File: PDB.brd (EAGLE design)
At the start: 130.3 x 166.9 mm, 55 parts, among them J1 B06B-HCMKK, J2 B06B-HCMKK, J3 SS-6488-NF-A431, J4 SS-6488-NF-A431, J5 B06B-HCMKK, J6 B03B-HCMKS, J7 B03B-HCMKS, J8 SS-6488-NF-A431

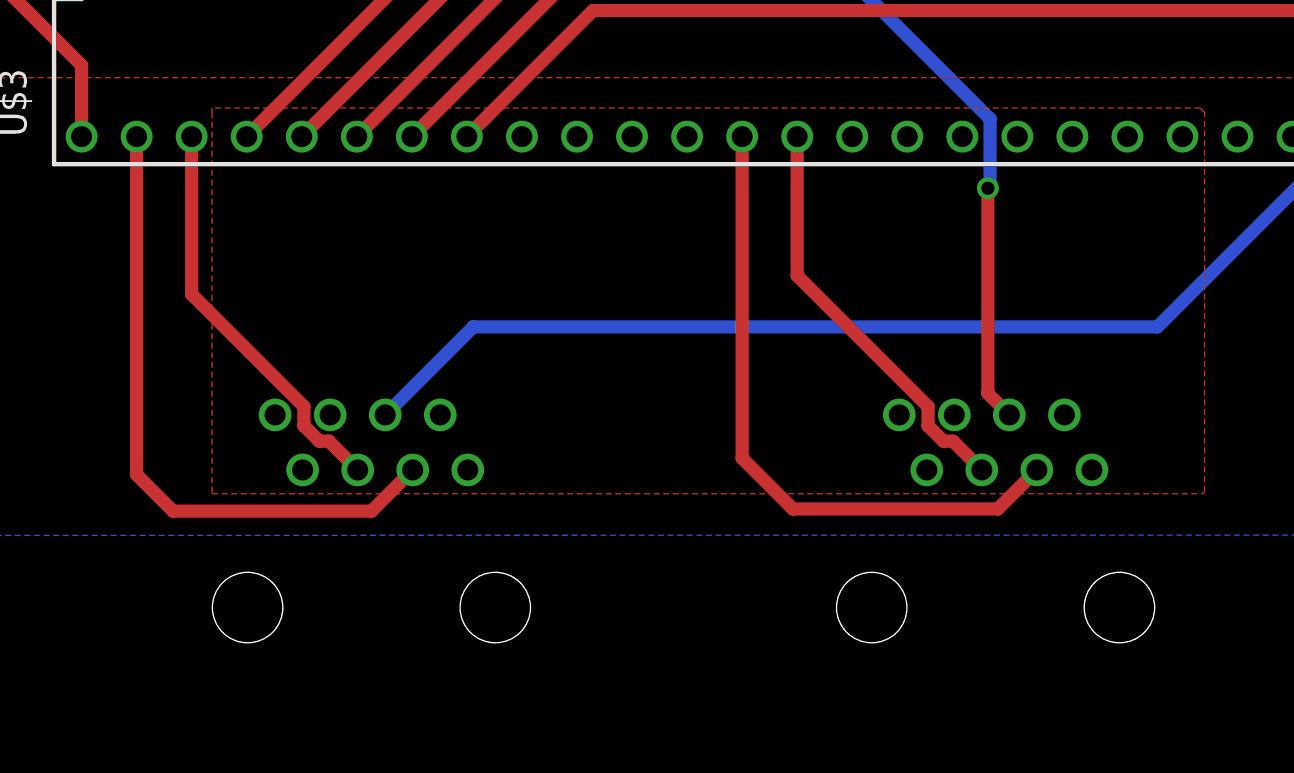
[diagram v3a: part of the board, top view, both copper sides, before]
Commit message: Adjusted schematic and routing to pass twisted pairs to each signal
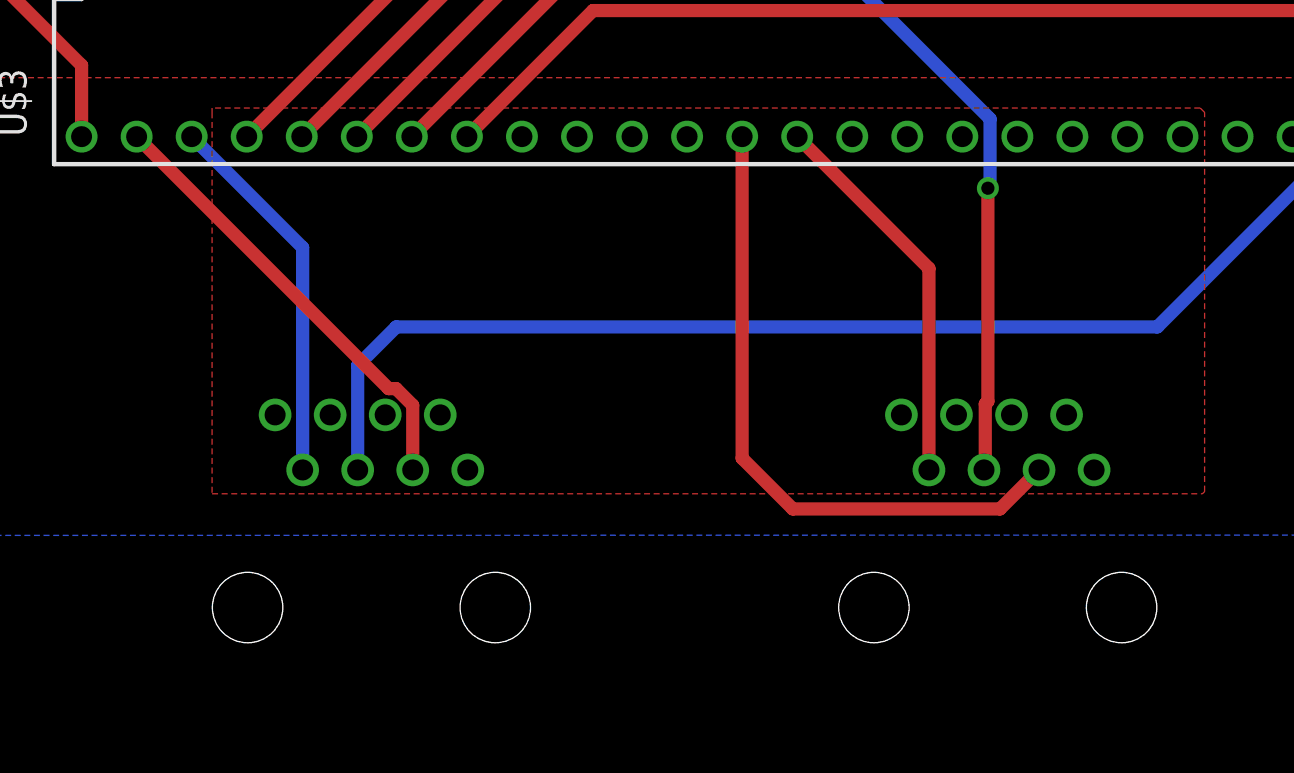
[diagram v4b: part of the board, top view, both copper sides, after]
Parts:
- moved J4 0.10 mm to (86.2, 6.70)
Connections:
- net CLK_A: now also J3.5; no longer J3.4
- net CLK_B: now also J4.5; no longer J4.4
- net GND: now also J3.4, J3.6, J3.8, J4.4, J4.6, J4.8
- net MISO_A: now also J3.7; no longer J3.5
- net MISO_B: now also J4.7; no longer J4.5
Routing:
- net MOSI_A: track 29.8 -> 20.9 mm
- net CLK_A: track 49.7 -> 54.9 mm
- net CLK_B: track 32.2 -> 34.4 mm
- net MISO_A: track 18.8 -> 17.5 mm
- net MISO_B: track 19.2 -> 17.9 mm
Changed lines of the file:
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@@
 <drawing>
 <settings>
-<setting alwaysvectorfont="no"/>
+<setting alwaysvectorfont="yes"/>
 <setting verticaltext="up"/>
 </settings>
@@
 <attribute name="VALUE" x="53.165" y="0.16" size="1.27" layer="28" rot="MR0" align="center"/>
 </element>
-<element name="J4" library="AUX Lib" package="SS6488NFA431" value="SS-6488-NF-A431" x="86.1" y="6.7" smashed="yes" rot="MR0">
-<attribute name="DESCRIPTION" value="Modular Connectors / Ethernet Connectors RJ45 Connector" x="86.1" y="6.7" size="1.778" layer="28" rot="MR0" display="off"/>
-<attribute name="HEIGHT" value="12.82mm" x="86.1" y="6.7" size="1.778" layer="28" rot="MR0" display="off"/>
-<attribute name="MANUFACTURER_NAME" value="Bel" x="86.1" y="6.7" size="1.778" layer="28" rot="MR0" display="off"/>
-<attribute name="MANUFACTURER_PART_NUMBER" value="SS-6488-NF-A431" x="86.1" y="6.7" size="1.778" layer="28" rot="MR0" display="off"/>
-<attribute name="MOUSER_PART_NUMBER" value="530-SS-6488-NF-A431" x="86.1" y="6.7" size="1.778" layer="28" rot="MR0" display="off"/>
-<attribute name="MOUSER_PRICE-STOCK" value="" x="86.1" y="6.7" size="1.778" layer="28" rot="MR0" display="off"/>
-<attribute name="NAME" x="81.965" y="0.16" size="1.27" layer="26" rot="MR0" align="center"/>
-<attribute name="VALUE" x="81.965" y="0.16" size="1.27" layer="28" rot="MR0" align="center"/>
+<element name="J4" library="AUX Lib" package="SS6488NFA431" value="SS-6488-NF-A431" x="86.2" y="6.7" smashed="yes" rot="MR0">
+<attribute name="DESCRIPTION" value="Modular Connectors / Ethernet Connectors RJ45 Connector" x="86.2" y="6.7" size="1.778" layer="28" rot="MR0" display="off"/>
+<attribute name="HEIGHT" value="12.82mm" x="86.2" y="6.7" size="1.778" layer="28" rot="MR0" display="off"/>
+<attribute name="MANUFACTURER_NAME" value="Bel" x="86.2" y="6.7" size="1.778" layer="28" rot="MR0" display="off"/>
+<attribute name="MANUFACTURER_PART_NUMBER" value="SS-6488-NF-A431" x="86.2" y="6.7" size="1.778" layer="28" rot="MR0" display="off"/>
+<attribute name="MOUSER_PART_NUMBER" value="530-SS-6488-NF-A431" x="86.2" y="6.7" size="1.778" layer="28" rot="MR0" display="off"/>
+<attribute name="MOUSER_PRICE-STOCK" value="" x="86.2" y="6.7" size="1.778" layer="28" rot="MR0" display="off"/>
+<attribute name="NAME" x="82.065" y="0.16" size="1.27" layer="26" rot="MR0" align="center"/>
+<attribute name="VALUE" x="82.065" y="0.16" size="1.27" layer="28" rot="MR0" align="center"/>
 </element>
 <element name="J5" library="AUX Lib" package="B06BHCMKK" value="B06B-HCMKK" x="92.1" y="54.4" smashed="yes" rot="MR0">
@@
 <wire x1="59.9" y1="142.3" x2="59.9" y2="143.34635" width="1.27" layer="16"/>
 <wire x1="59.9" y1="143.34635" x2="56.19535" y2="147.051" width="1.27" layer="16"/>
-<wire x1="27.4532" y1="115.1" x2="29.55" y2="117.8" width="0" layer="19" extent="1-1"/>
-<wire x1="12.14" y1="89.33" x2="27.4532" y2="115.1" width="0" layer="19" extent="1-1"/>
-<wire x1="12.3" y1="81.512" x2="12.14" y2="89.33" width="0" layer="19" extent="1-1"/>
-<wire x1="12.3" y1="76.432" x2="12.3" y2="81.512" width="0" layer="19" extent="1-1"/>
 </signal>
 <signal name="HAZ_L_SIG">
@@
 <wire x1="112.8" y1="48.05" x2="109.967" y2="48.05" width="1.27" layer="1"/>
 <wire x1="109.967" y1="48.05" x2="109.914" y2="48.103" width="1.27" layer="1"/>
+<contactref element="J3" pad="4"/>
+<contactref element="J3" pad="6"/>
+<contactref element="J3" pad="8"/>
+<contactref element="J4" pad="4"/>
+<contactref element="J4" pad="6"/>
+<contactref element="J4" pad="8"/>
 </signal>
 <signal name="AGND">
@@
 <wire x1="45.61" y1="107.72218125" x2="67.68781875" y2="129.8" width="1.5" layer="16"/>
 <wire x1="67.68781875" y1="129.8" x2="84.40898125" y2="129.8" width="1.5" layer="16"/>
-<wire x1="33.588" y1="49.7" x2="38.668" y2="49.7" width="0" layer="19" extent="1-1"/>
-<wire x1="33.6" y1="52.65" x2="33.588" y2="49.7" width="0" layer="19" extent="1-1"/>
-<wire x1="31.2" y1="51.8" x2="33.6" y2="52.65" width="0" layer="19" extent="1-1"/>
 </signal>
 <signal name="N$10">
@@
 <contactref element="J3" pad="3"/>
 <contactref element="U$3" pad="0"/>
-<wire x1="42.02" y1="22.08" x2="42.02" y2="6.48" width="0.6096" layer="1"/>
-<wire x1="42.02" y1="6.48" x2="43.7" y2="4.8" width="0.6096" layer="1"/>
-<wire x1="43.7" y1="4.8" x2="52.86" y2="4.8" width="0.6096" layer="1"/>
-<wire x1="52.86" y1="4.8" x2="54.76" y2="6.7" width="0.6096" layer="1"/>
+<wire x1="42.02" y1="22.08" x2="53.6483" y2="10.4517" width="0.6096" layer="1"/>
+<wire x1="53.6483" y1="10.4517" x2="53.99190625" y2="10.4517" width="0.6096" layer="1"/>
+<wire x1="53.99190625" y1="10.4517" x2="54.76" y2="9.68360625" width="0.6096" layer="1"/>
+<wire x1="54.76" y1="9.68360625" x2="54.76" y2="6.7" width="0.6096" layer="1"/>
 </signal>
 <signal name="CLK_A">
-<contactref element="J3" pad="4"/>
 <contactref element="U$3" pad="32"/>
 <wire x1="97.9" y1="22.08" x2="89.12" y2="13.3" width="0.6096" layer="16"/>
-<wire x1="57.55" y1="13.3" x2="53.49" y2="9.24" width="0.6096" layer="16"/>
-<wire x1="89.12" y1="13.3" x2="57.55" y2="13.3" width="0.6096" layer="16"/>
+<contactref element="J3" pad="5"/>
+<wire x1="52.22" y1="11.52" x2="52.22" y2="6.7" width="0.6096" layer="16"/>
+<wire x1="89.12" y1="13.3" x2="54" y2="13.3" width="0.6096" layer="16"/>
+<wire x1="54" y1="13.3" x2="52.22" y2="11.52" width="0.6096" layer="16"/>
 </signal>
 <signal name="MISO_A">
-<contactref element="J3" pad="5"/>
 <contactref element="U$3" pad="1"/>
-<wire x1="49.7383" y1="8.73809375" x2="50.44809375" y2="8.0283" width="0.6096" layer="1"/>
-<wire x1="50.44809375" y1="8.0283" x2="50.8917" y2="8.0283" width="0.6096" layer="1"/>
-<wire x1="50.8917" y1="8.0283" x2="52.22" y2="6.7" width="0.6096" layer="1"/>
-<wire x1="44.56" y1="22.08" x2="44.56" y2="14.80360625" width="0.6096" layer="1"/>
-<wire x1="44.56" y1="14.80360625" x2="49.7383" y2="9.62530625" width="0.6096" layer="1"/>
-<wire x1="49.7383" y1="9.62530625" x2="49.7383" y2="8.73809375" width="0.6096" layer="1"/>
+<contactref element="J3" pad="7"/>
+<wire x1="44.56" y1="22.08" x2="49.68" y2="16.96" width="0.6096" layer="16"/>
+<wire x1="49.68" y1="16.96" x2="49.68" y2="6.7" width="0.6096" layer="16"/>
 </signal>
 <signal name="MOSI_B">
@@
 <wire x1="69.96" y1="22.08" x2="69.96" y2="7.24" width="0.6096" layer="1"/>
 <wire x1="69.96" y1="7.24" x2="72.3" y2="4.9" width="0.6096" layer="1"/>
-<wire x1="72.3" y1="4.9" x2="81.76" y2="4.9" width="0.6096" layer="1"/>
-<wire x1="81.76" y1="4.9" x2="83.56" y2="6.7" width="0.6096" layer="1"/>
+<wire x1="72.3" y1="4.9" x2="81.86" y2="4.9" width="0.6096" layer="1"/>
+<wire x1="81.86" y1="4.9" x2="83.66" y2="6.7" width="0.6096" layer="1"/>
 </signal>
 <signal name="MISO_B">
-<contactref element="J4" pad="5"/>
 <contactref element="U$3" pad="12"/>
-<wire x1="78.5383" y1="8.73809375" x2="79.24809375" y2="8.0283" width="0.6096" layer="1"/>
-<wire x1="79.24809375" y1="8.0283" x2="79.6917" y2="8.0283" width="0.6096" layer="1"/>
-<wire x1="79.6917" y1="8.0283" x2="81.02" y2="6.7" width="0.6096" layer="1"/>
-<wire x1="72.5" y1="22.08" x2="72.5" y2="15.66360625" width="0.6096" layer="1"/>
-<wire x1="72.5" y1="15.66360625" x2="78.5383" y2="9.62530625" width="0.6096" layer="1"/>
-<wire x1="78.5383" y1="9.62530625" x2="78.5383" y2="8.73809375" width="0.6096" layer="1"/>
+<contactref element="J4" pad="7"/>
+<wire x1="72.5" y1="22.08" x2="78.58" y2="16" width="0.6096" layer="1"/>
+<wire x1="78.58" y1="16" x2="78.58" y2="6.7" width="0.6096" layer="1"/>
 </signal>
 <signal name="CLK_B">
-<contactref element="J4" pad="4"/>
 <contactref element="U$3" pad="13"/>
 <wire x1="72.5" y1="37.32" x2="72.5" y2="31.8" width="0.6096" layer="16"/>
@@
 <wire x1="81.4" y1="19.8" x2="81.3" y2="19.7" width="0.6096" layer="16"/>
 <via x="81.3" y="19.7" extent="1-16" drill="0.6096"/>
-<wire x1="81.3" y1="19.7" x2="81.3" y2="10.23" width="0.6096" layer="1"/>
-<wire x1="81.3" y1="10.23" x2="82.29" y2="9.24" width="0.6096" layer="1"/>
+<contactref element="J4" pad="5"/>
+<wire x1="81.3" y1="19.7" x2="81.3" y2="9.86360625" width="0.6096" layer="1"/>
+<wire x1="81.3" y1="9.86360625" x2="81.1783" y2="9.74190625" width="0.6096" layer="1"/>
+<wire x1="81.1783" y1="6.7583" x2="81.12" y2="6.7" width="0.6096" layer="1"/>
+<wire x1="81.1783" y1="9.74190625" x2="81.1783" y2="6.7583" width="0.6096" layer="1"/>
 </signal>
 <signal name="H9">

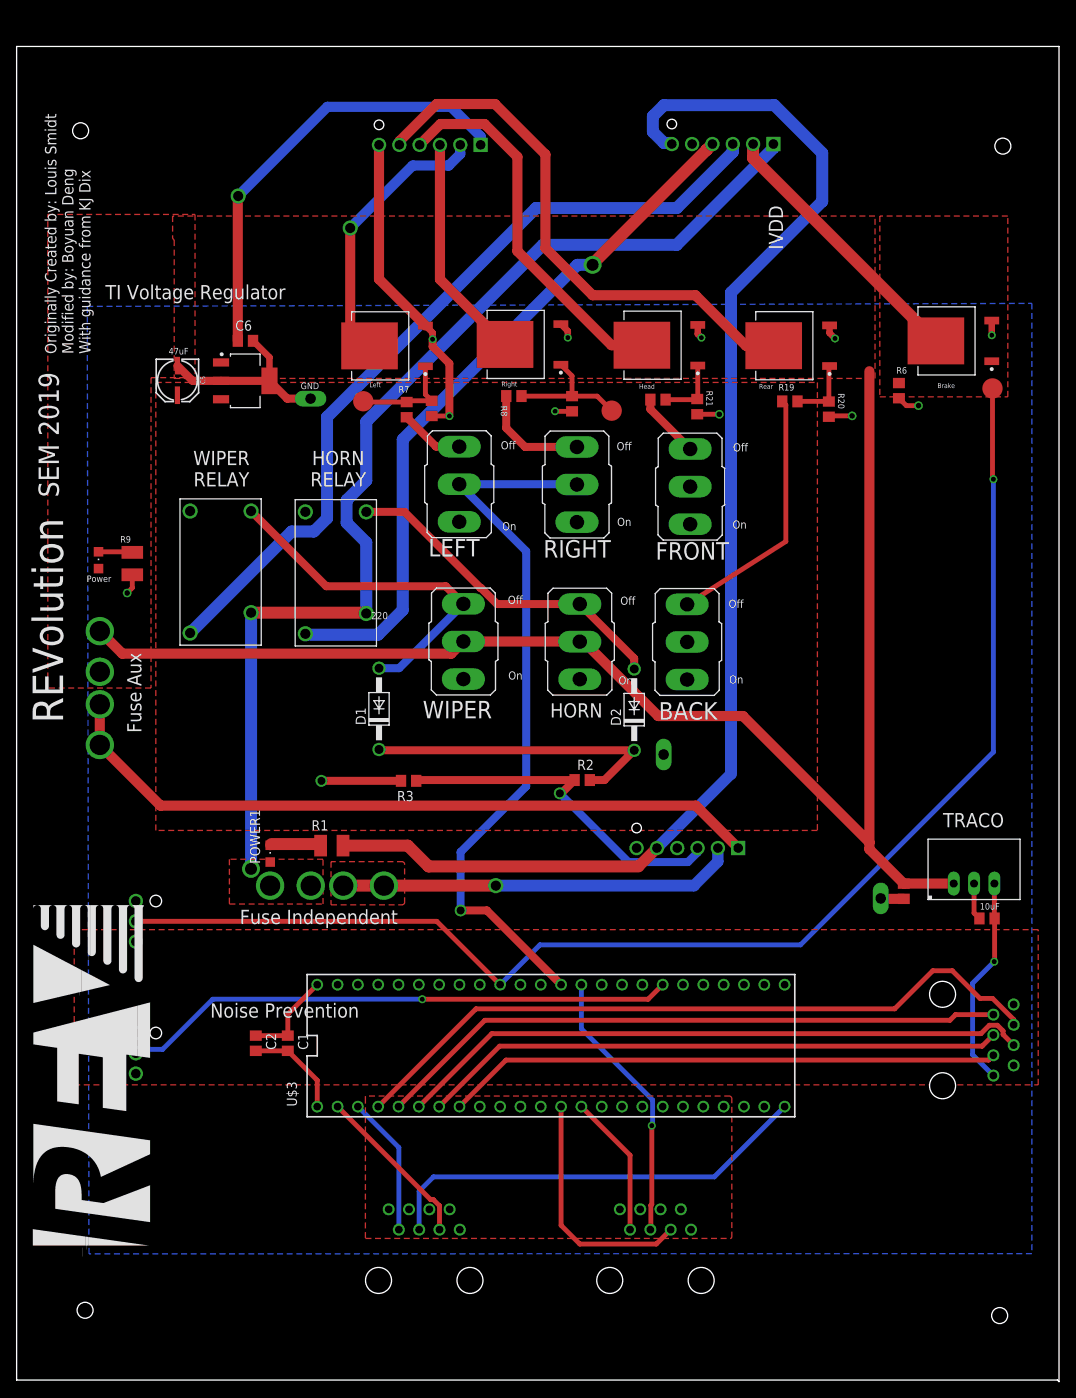
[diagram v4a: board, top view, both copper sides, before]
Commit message: switched order of output bus
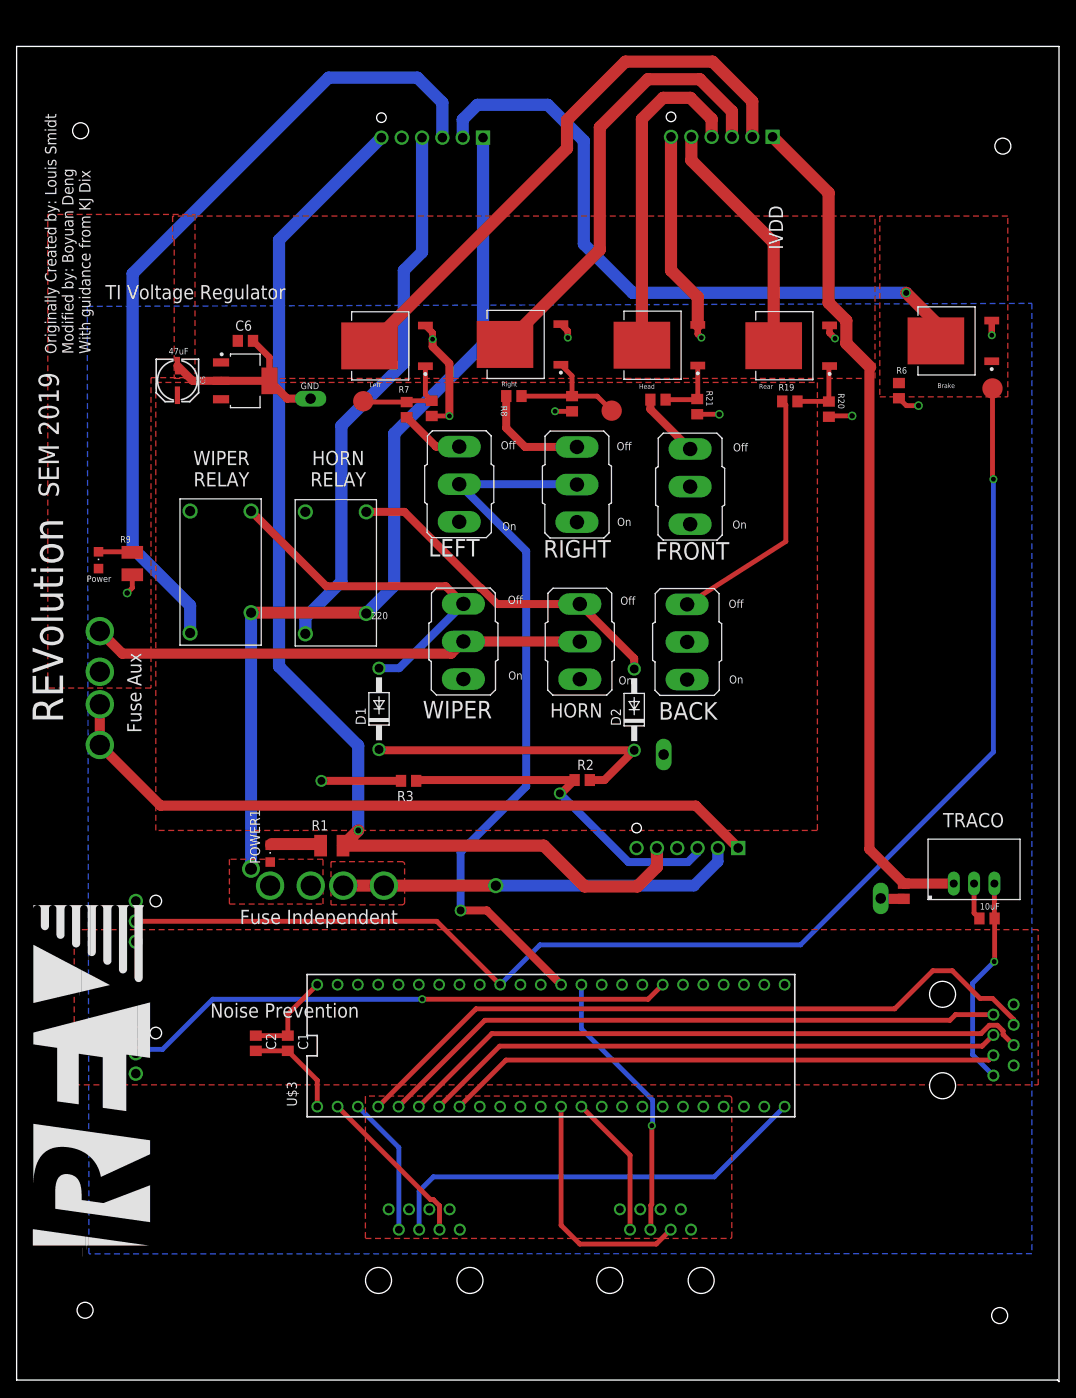
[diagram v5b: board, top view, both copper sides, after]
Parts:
- moved J1 36.5 mm to (96.4, 143.3)
- moved J2 36.3 mm to (60.2, 143.2)
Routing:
- net VDD: track 236.1 -> 168.2 mm, vias 1 -> 0
- net BRAKE_SIG: track 34.1 -> 83.3 mm, vias 0 -> 1
- net REARLIGHT_SIG: track 68.5 -> 30.4 mm
- net HAZ_L_SIG: track 34.5 -> 71.1 mm, vias 1 -> 0
- net HAZ_R_SIG: track 28.3 -> 55.9 mm
- net IVDD: track 138.1 -> 112.0 mm
- net IGND: track 165.9 -> 143.4 mm, vias 0 -> 1
- net HORN: track 88.9 -> 68.1 mm, vias 1 -> 0
- net HEADLIGHT_SIG: track 47.2 -> 41.4 mm
- net WIPER: track 101.2 -> 102.4 mm
